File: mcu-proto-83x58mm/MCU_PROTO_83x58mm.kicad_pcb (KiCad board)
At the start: 2 copper layers, 75 x 49 mm, 213 parts, among them J1 Screw_Terminal_01x03, J10 Conn_01x20_Female, J11 Conn_01x01_Male, J12 Conn_01x01_Male, J2 Screw_Terminal_01x03, J3 Conn_01x20_Female, J4 Conn_01x20_Female, J5 Conn_01x20_Female, J6 Conn_01x20_Female, J7 Conn_01x20_Female, J8 Conn_01x20_Female, J9 Conn_01x20_Female

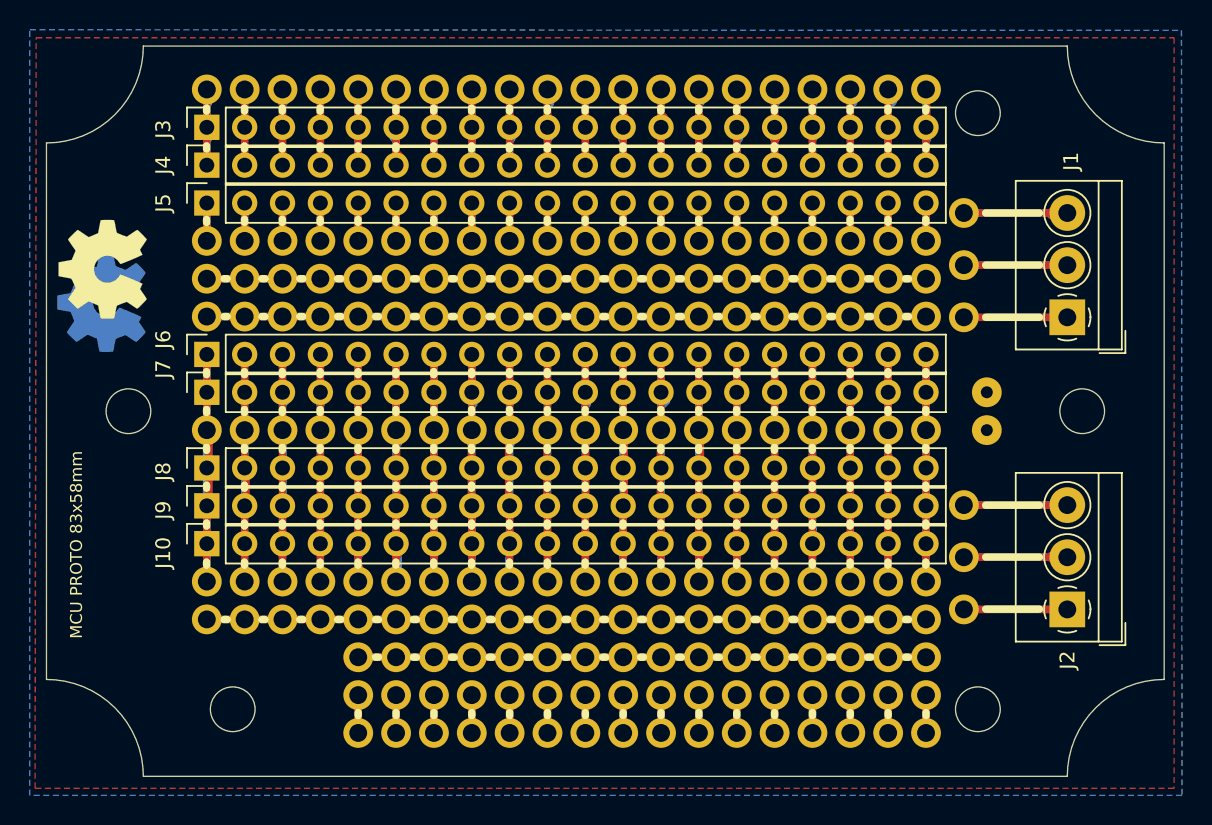
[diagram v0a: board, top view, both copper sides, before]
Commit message: Update MCU_PROTO_83x58mm: PCB improvements and Gerber file regeneration
- Updated main PCB file (MCU_PROTO_83x58mm.kicad_pcb) with design improvements
- Regenerated all Gerber files for single board (copper, mask, silkscreen, drills)
- Updated panel Gerber files with new naming convention
- Replaced old silkscreen files (B_SilkS/F_SilkS) with new Silkscreen versions
- Removed obsolete SVG visualization files
- Added new KiCad project files (.kicad_prl, .kicad_pro, .kicad_sch)
- Added custom library with pad and silkscreen footprints
- Updated footprint library cache and table
- Added backup files from recent design iterations
- Generated new Gerber ZIP archives for single and panel boards
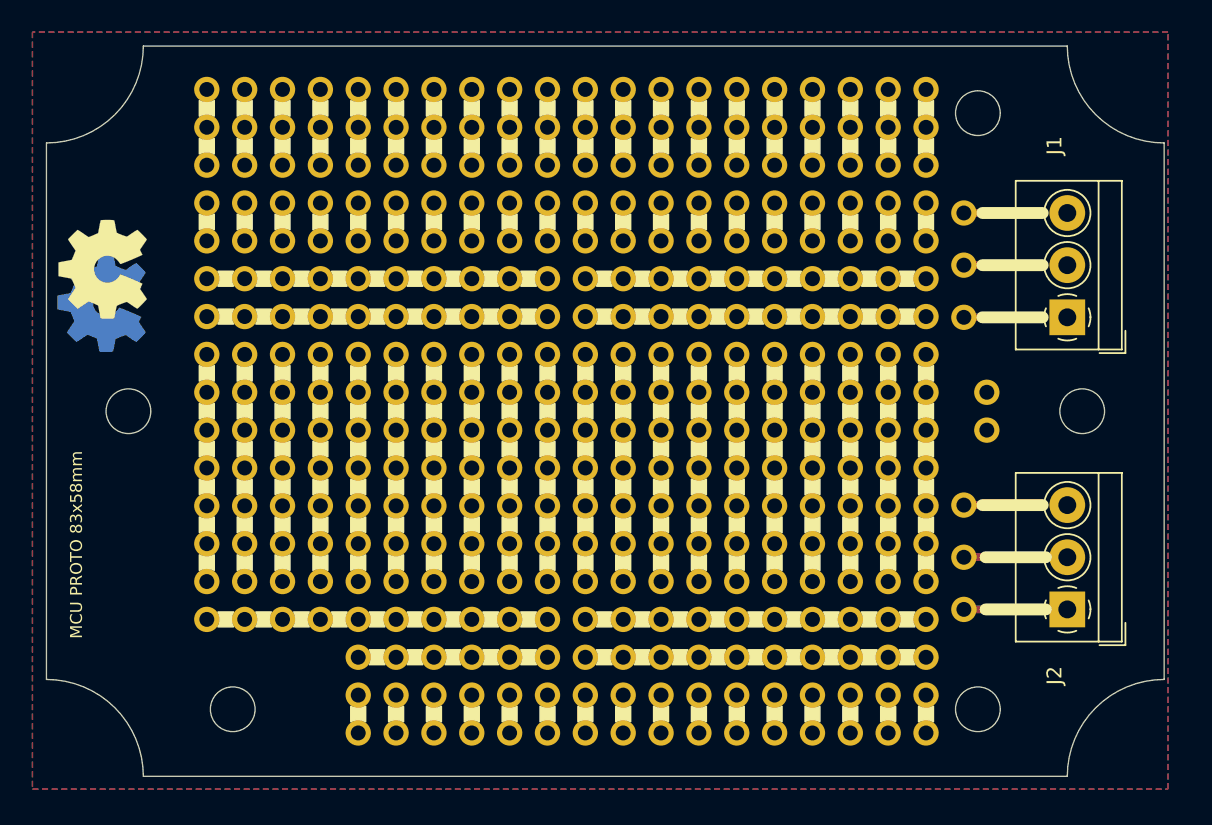
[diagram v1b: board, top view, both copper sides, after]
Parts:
- removed H2, H3, H4, H5, H6: MountingHole, MountingHole:MountingHole_3mm
- removed J10, J3, J4, J5, J6, J7, J8, J9: Conn_01x20_Female, Connector_PinSocket_2.54mm:PinSocket_1x20_P2.54mm_Vertical
- removed the REF** at (110.8, 113.1)
- removed the REF** at (138.7, 125.8)
- removed the REF** at (143.8, 118.2)
- removed the REF** at (141.2, 118.2)
- removed the REF** at (138.7, 118.2)
- removed the REF** at (136.2, 118.2)
- removed the REF** at (133.6, 118.2)
- removed the REF** at (131.1, 118.2)
- removed the REF** at (128.5, 118.2)
- removed the REF** at (126.0, 118.2)
- removed the REF** at (123.5, 118.2)
- removed the REF** at (120.9, 118.2)
- removed the REF** at (136.2, 125.8)
- removed the REF** at (118.4, 118.2)
- removed the REF** at (115.8, 118.2)
- removed the REF** at (113.3, 118.2)
- removed the REF** at (110.8, 118.2)
- removed the REF** at (159.0, 115.6)
- removed the REF** at (156.5, 115.6)
- removed the REF** at (153.9, 115.6)
- removed the REF** at (151.4, 115.6)
- removed the REF** at (148.9, 115.6)
- removed the REF** at (146.3, 115.6)
- removed the REF** at (133.6, 125.8)
- removed the REF** at (143.8, 115.6)
- removed the REF** at (141.2, 115.6)
- removed the REF** at (138.7, 115.6)
- removed the REF** at (136.2, 115.6)
- removed the REF** at (133.6, 115.6)
- removed the REF** at (131.1, 115.6)
- removed the REF** at (128.5, 115.6)
- removed the REF** at (126.0, 115.6)
- removed the REF** at (123.5, 115.6)
- removed the REF** at (120.9, 115.6)
- removed the REF** at (131.1, 125.8)
- removed the REF** at (118.4, 115.6)
- removed the REF** at (115.8, 115.6)
- removed the REF** at (113.3, 115.6)
- removed the REF** at (110.8, 115.6)
- removed the REF** at (159.0, 113.1)
- removed the REF** at (156.5, 113.1)
- removed the REF** at (153.9, 113.1)
- removed the REF** at (151.4, 113.1)
- removed the REF** at (148.9, 113.1)
- removed the REF** at (146.3, 113.1)
- removed the REF** at (128.5, 125.8)
- removed the REF** at (143.8, 113.1)
- removed the REF** at (141.2, 113.1)
- removed the REF** at (138.7, 113.1)
- removed the REF** at (136.2, 113.1)
- removed the REF** at (133.6, 113.1)
- removed the REF** at (131.1, 113.1)
- removed the REF** at (128.5, 113.1)
- removed the REF** at (126.0, 113.1)
- removed the REF** at (123.5, 113.1)
- removed the REF** at (120.9, 113.1)
- removed the REF** at (126.0, 125.8)
- removed the REF** at (118.4, 113.1)
- removed the REF** at (115.8, 113.1)
- removed the REF** at (113.3, 113.1)
- removed the REF** at (110.8, 102.9)
- removed the REF** at (113.3, 102.9)
- removed the REF** at (115.8, 102.9)
- removed the REF** at (118.4, 102.9)
- removed the REF** at (120.9, 102.9)
- removed the REF** at (123.5, 102.9)
- removed the REF** at (123.5, 146.1)
- removed the REF** at (123.5, 125.8)
- removed the REF** at (120.9, 146.1)
- removed the REF** at (159.0, 146.1)
- removed the REF** at (156.5, 146.1)
- removed the REF** at (138.7, 146.1)
- removed the REF** at (146.3, 146.1)
- removed the REF** at (141.2, 146.1)
- removed the REF** at (136.2, 146.1)
- removed the REF** at (133.6, 146.1)
- removed the REF** at (131.1, 146.1)
- removed the REF** at (128.5, 146.1)
- removed the REF** at (120.9, 125.8)
- removed the REF** at (126.0, 146.1)
- removed the REF** at (143.8, 146.1)
- removed the REF** at (148.9, 146.1)
- removed the REF** at (153.9, 146.1)
- removed the REF** at (151.4, 146.1)
- removed the REF** at (146.3, 102.9)
- removed the REF** at (159.0, 102.9)
- removed the REF** at (156.5, 102.9)
- removed the REF** at (153.9, 102.9)
- removed the REF** at (151.4, 102.9)
- removed the REF** at (118.4, 125.8)
- removed the REF** at (148.9, 102.9)
- removed the REF** at (161.6, 114.7)
- removed the REF** at (161.6, 137.8)
- removed the REF** at (161.6, 134.3)
- removed the REF** at (161.6, 130.8)
- removed the REF** at (161.6, 118.2)
- removed the REF** at (161.6, 111.2)
- removed the REF** at (143.8, 102.9)
- removed the REF** at (141.2, 102.9)
- removed the REF** at (138.7, 102.9)
- removed the REF** at (115.8, 125.8)
- removed the REF** at (136.2, 102.9)
- removed the REF** at (133.6, 102.9)
- removed the REF** at (131.1, 102.9)
- removed the REF** at (128.5, 102.9)
- removed the REF** at (126.0, 102.9)
- removed the REF** at (159.0, 125.8)
- removed the REF** at (113.3, 125.8)
- removed the REF** at (110.8, 125.8)
- removed the REF** at (159.0, 143.6)
- removed the REF** at (156.5, 143.6)
- removed the REF** at (153.9, 143.6)
- removed the REF** at (151.4, 143.6)
- removed the REF** at (148.9, 143.6)
- removed the REF** at (146.3, 143.6)
- removed the REF** at (143.8, 143.6)
- removed the REF** at (141.2, 143.6)
- removed the REF** at (156.5, 125.8)
- removed the REF** at (138.7, 143.6)
- removed the REF** at (136.2, 143.6)
- removed the REF** at (133.6, 143.6)
- removed the REF** at (131.1, 143.6)
- removed the REF** at (128.5, 143.6)
- removed the REF** at (126.0, 143.6)
- removed the REF** at (123.5, 143.6)
- removed the REF** at (120.9, 143.6)
- removed the REF** at (159.0, 141.0)
- removed the REF** at (156.5, 141.0)
- removed the REF** at (153.9, 125.8)
- removed the REF** at (153.9, 141.0)
- removed the REF** at (151.4, 141.0)
- removed the REF** at (148.9, 141.0)
- removed the REF** at (146.3, 141.0)
- removed the REF** at (143.8, 141.0)
- removed the REF** at (141.2, 141.0)
- removed the REF** at (138.7, 141.0)
- removed the REF** at (136.2, 141.0)
- removed the REF** at (133.6, 141.0)
- removed the REF** at (131.1, 141.0)
- removed the REF** at (151.4, 125.8)
- removed the REF** at (128.5, 141.0)
- removed the REF** at (126.0, 141.0)
- removed the REF** at (123.5, 141.0)
- removed the REF** at (120.9, 141.0)
- removed the REF** at (159.0, 138.5)
- removed the REF** at (156.5, 138.5)
- removed the REF** at (153.9, 138.5)
- removed the REF** at (151.4, 138.5)
- removed the REF** at (148.9, 138.5)
- removed the REF** at (146.3, 138.5)
- removed the REF** at (148.9, 125.8)
- removed the REF** at (143.8, 138.5)
- removed the REF** at (141.2, 138.5)
- removed the REF** at (138.7, 138.5)
- removed the REF** at (136.2, 138.5)
- removed the REF** at (133.6, 138.5)
- removed the REF** at (131.1, 138.5)
- removed the REF** at (128.5, 138.5)
- removed the REF** at (126.0, 138.5)
- removed the REF** at (123.5, 138.5)
- removed the REF** at (120.9, 138.5)
- removed the REF** at (146.3, 125.8)
- removed the REF** at (118.4, 138.5)
- removed the REF** at (115.8, 138.5)
- removed the REF** at (113.3, 138.5)
- removed the REF** at (110.8, 138.5)
- removed the REF** at (159.0, 135.9)
- removed the REF** at (156.5, 135.9)
- removed the REF** at (153.9, 135.9)
- removed the REF** at (151.4, 135.9)
- removed the REF** at (148.9, 135.9)
- removed the REF** at (146.3, 135.9)
- removed the REF** at (143.8, 125.8)
- removed the REF** at (143.8, 135.9)
- removed the REF** at (141.2, 135.9)
- removed the REF** at (138.7, 135.9)
- removed the REF** at (136.2, 135.9)
- removed the REF** at (133.6, 135.9)
- removed the REF** at (131.1, 135.9)
- removed the REF** at (128.5, 135.9)
- removed the REF** at (126.0, 135.9)
- removed the REF** at (123.5, 135.9)
- removed the REF** at (120.9, 135.9)
- removed the REF** at (141.2, 125.8)
- removed the REF** at (118.4, 135.9)
- removed the REF** at (115.8, 135.9)
- removed the REF** at (113.3, 135.9)
- removed the REF** at (110.8, 135.9)
- removed the REF** at (159.0, 118.2)
- removed the REF** at (156.5, 118.2)
- removed the REF** at (153.9, 118.2)
- removed the REF** at (151.4, 118.2)
- removed the REF** at (148.9, 118.2)
- removed the REF** at (146.3, 118.2)
- added REF**: Round_Pad_1.7mm_Hole_1.0mm, proto-pcb-pads:RoundPad_1.7mm_Hole_1.0mm, F.Cu at (133.6, 118.2)
- added REF**: Pad_Link_1.7mm_Width_1.0mm, proto-pcb-silks:PadLink_1.7mm_Width_1.0mm, F.Cu at (138.7, 130.8)
- added REF**: Round_Pad_1.7mm_Hole_1.0mm, proto-pcb-pads:RoundPad_1.7mm_Hole_1.0mm, F.Cu at (159.0, 141.0)
- added REF**: Round_Pad_1.7mm_Hole_1.0mm, proto-pcb-pads:RoundPad_1.7mm_Hole_1.0mm, F.Cu at (141.2, 146.1)
- added REF**: Round_Pad_1.7mm_Hole_1.0mm, proto-pcb-pads:RoundPad_1.7mm_Hole_1.0mm, F.Cu at (153.9, 125.8)
- added REF**: Round_Pad_1.7mm_Hole_1.0mm, proto-pcb-pads:RoundPad_1.7mm_Hole_1.0mm, F.Cu at (143.8, 143.6)
- added REF**: Round_Pad_1.7mm_Hole_1.0mm, proto-pcb-pads:RoundPad_1.7mm_Hole_1.0mm, F.Cu at (156.5, 115.6)
- added REF**: Round_Pad_1.7mm_Hole_1.0mm, proto-pcb-pads:RoundPad_1.7mm_Hole_1.0mm, F.Cu at (153.9, 141.0)
- added REF**: Pad_Link_1.7mm_Width_1.0mm, proto-pcb-silks:PadLink_1.7mm_Width_1.0mm, F.Cu at (153.9, 138.5)
- added REF**: Round_Pad_1.7mm_Hole_1.0mm, proto-pcb-pads:RoundPad_1.7mm_Hole_1.0mm, F.Cu at (136.2, 123.2)
- added REF**: Round_Pad_1.7mm_Hole_1.0mm, proto-pcb-pads:RoundPad_1.7mm_Hole_1.0mm, F.Cu at (110.8, 135.9)
- added REF**: Round_Pad_1.7mm_Hole_1.0mm, proto-pcb-pads:RoundPad_1.7mm_Hole_1.0mm, F.Cu at (126.0, 123.2)
- added REF**: Pad_Link_1.7mm_Width_1.0mm, proto-pcb-silks:PadLink_1.7mm_Width_1.0mm, F.Cu at (151.4, 115.6)
- added REF**: Pad_Link_1.7mm_Width_1.0mm, proto-pcb-silks:PadLink_1.7mm_Width_1.0mm, F.Cu at (141.2, 141.0)
- added REF**: Pad_Link_1.7mm_Width_1.0mm, proto-pcb-silks:PadLink_1.7mm_Width_1.0mm, F.Cu at (151.4, 141.0)
- added REF**: Pad_Link_1.7mm_Width_1.0mm, proto-pcb-silks:PadLink_1.7mm_Width_1.0mm, F.Cu at (138.7, 105.5)
- added REF**: Pad_Link_1.7mm_Width_1.0mm, proto-pcb-silks:PadLink_1.7mm_Width_1.0mm, F.Cu at (113.3, 120.7)
- added REF**: MountingHole_3mm, MountingHole:MountingHole_3mm, F.Cu at (162.5, 104.5)
- added REF**: Round_Pad_1.7mm_Hole_1.0mm, proto-pcb-pads:RoundPad_1.7mm_Hole_1.0mm, F.Cu at (126.0, 133.4)
- added REF**: Round_Pad_1.7mm_Hole_1.0mm, proto-pcb-pads:RoundPad_1.7mm_Hole_1.0mm, F.Cu at (126.0, 120.7)
- added REF**: Round_Pad_1.7mm_Hole_1.0mm, proto-pcb-pads:RoundPad_1.7mm_Hole_1.0mm, F.Cu at (120.9, 128.3)
- added REF**: Pad_Link_1.7mm_Width_1.0mm, proto-pcb-silks:PadLink_1.7mm_Width_1.0mm, F.Cu at (115.8, 138.5)
- added REF**: Pad_Link_1.7mm_Width_1.0mm, proto-pcb-silks:PadLink_1.7mm_Width_1.0mm, F.Cu at (153.9, 133.4)
- added REF**: Round_Pad_1.7mm_Hole_1.0mm, proto-pcb-pads:RoundPad_1.7mm_Hole_1.0mm, F.Cu at (123.5, 128.3)
- added REF**: Pad_Link_1.7mm_Width_1.0mm, proto-pcb-silks:PadLink_1.7mm_Width_1.0mm, F.Cu at (143.8, 123.2)
- added REF**: Round_Pad_1.7mm_Hole_1.0mm, proto-pcb-pads:RoundPad_1.7mm_Hole_1.0mm, F.Cu at (148.9, 143.6)
- added REF**: Round_Pad_1.7mm_Hole_1.0mm, proto-pcb-pads:RoundPad_1.7mm_Hole_1.0mm, F.Cu at (151.4, 115.6)
- added REF**: Round_Pad_1.7mm_Hole_1.0mm, proto-pcb-pads:RoundPad_1.7mm_Hole_1.0mm, F.Cu at (153.9, 115.6)
- added REF**: Pad_Link_1.7mm_Width_1.0mm, proto-pcb-silks:PadLink_1.7mm_Width_1.0mm, F.Cu at (143.8, 120.7)
- added REF**: Round_Pad_1.7mm_Hole_1.0mm, proto-pcb-pads:RoundPad_1.7mm_Hole_1.0mm, F.Cu at (115.8, 128.3)
- added REF**: Pad_Link_1.7mm_Width_1.0mm, proto-pcb-silks:PadLink_1.7mm_Width_1.0mm, F.Cu at (113.3, 138.5)
- added REF**: Round_Pad_1.7mm_Hole_1.0mm, proto-pcb-pads:RoundPad_1.7mm_Hole_1.0mm, F.Cu at (136.2, 125.8)
- added REF**: Pad_Link_1.7mm_Width_1.0mm, proto-pcb-silks:PadLink_1.7mm_Width_1.0mm, F.Cu at (128.5, 125.8)
- added REF**: Pad_Link_1.7mm_Width_1.0mm, proto-pcb-silks:PadLink_1.7mm_Width_1.0mm, F.Cu at (151.4, 123.2)
- added REF**: Pad_Link_1.7mm_Width_1.0mm, proto-pcb-silks:PadLink_1.7mm_Width_1.0mm, F.Cu at (123.5, 133.4)
- added REF**: Pad_Link_1.7mm_Width_1.0mm, proto-pcb-silks:PadLink_1.7mm_Width_1.0mm, F.Cu at (131.1, 123.2)
- added REF**: Pad_Link_1.7mm_Width_1.0mm, proto-pcb-silks:PadLink_1.7mm_Width_1.0mm, F.Cu at (110.8, 128.3)
- added REF**: Round_Pad_1.7mm_Hole_1.0mm, proto-pcb-pads:RoundPad_1.7mm_Hole_1.0mm, F.Cu at (120.9, 102.9)
- added REF**: Pad_Link_1.7mm_Width_1.0mm, proto-pcb-silks:PadLink_1.7mm_Width_1.0mm, F.Cu at (133.6, 102.9)
- added REF**: Round_Pad_1.7mm_Hole_1.0mm, proto-pcb-pads:RoundPad_1.7mm_Hole_1.0mm, F.Cu at (146.3, 102.9)
- added REF**: Pad_Link_1.7mm_Width_1.0mm, proto-pcb-silks:PadLink_1.7mm_Width_1.0mm, F.Cu at (148.9, 138.5)
- added REF**: Round_Pad_1.7mm_Hole_1.0mm, proto-pcb-pads:RoundPad_1.7mm_Hole_1.0mm, F.Cu at (148.9, 146.1)
- added REF**: Pad_Link_1.7mm_Width_1.0mm, proto-pcb-silks:PadLink_1.7mm_Width_1.0mm, F.Cu at (133.6, 105.5)
- added REF**: Pad_Link_1.7mm_Width_1.0mm, proto-pcb-silks:PadLink_1.7mm_Width_1.0mm, F.Cu at (113.3, 110.5)
- added REF**: Pad_Link_1.7mm_Width_1.0mm, proto-pcb-silks:PadLink_1.7mm_Width_1.0mm, F.Cu at (118.4, 123.2)
- added REF**: Round_Pad_1.7mm_Hole_1.0mm, proto-pcb-pads:RoundPad_1.7mm_Hole_1.0mm, F.Cu at (141.2, 128.3)
- added REF**: Round_Pad_1.7mm_Hole_1.0mm, proto-pcb-pads:RoundPad_1.7mm_Hole_1.0mm, F.Cu at (110.8, 128.3)
- added REF**: Pad_Link_1.7mm_Width_1.0mm, proto-pcb-silks:PadLink_1.7mm_Width_1.0mm, F.Cu at (159.0, 102.9)
- added REF**: Pad_Link_1.7mm_Width_1.0mm, proto-pcb-silks:PadLink_1.7mm_Width_1.0mm, F.Cu at (159.0, 105.5)
- added REF**: Round_Pad_1.7mm_Hole_1.0mm, proto-pcb-pads:RoundPad_1.7mm_Hole_1.0mm, F.Cu at (136.2, 146.1)
- added REF**: Round_Pad_1.7mm_Hole_1.0mm, proto-pcb-pads:RoundPad_1.7mm_Hole_1.0mm, F.Cu at (148.9, 138.5)
- added REF**: Pad_Link_1.7mm_Width_1.0mm, proto-pcb-silks:PadLink_1.7mm_Width_1.0mm, F.Cu at (123.5, 110.5)
- added REF**: Pad_Link_1.7mm_Width_1.0mm, proto-pcb-silks:PadLink_1.7mm_Width_1.0mm, F.Cu at (143.8, 133.4)
- added REF**: Round_Pad_1.7mm_Hole_1.0mm, proto-pcb-pads:RoundPad_1.7mm_Hole_1.0mm, F.Cu at (131.1, 108.0)
- added REF**: Round_Pad_1.7mm_Hole_1.0mm, proto-pcb-pads:RoundPad_1.7mm_Hole_1.0mm, F.Cu at (146.3, 108.0)
- added REF**: Round_Pad_1.7mm_Hole_1.0mm, proto-pcb-pads:RoundPad_1.7mm_Hole_1.0mm, F.Cu at (146.3, 138.5)
- added REF**: Pad_Link_1.7mm_Width_1.0mm, proto-pcb-silks:PadLink_1.7mm_Width_1.0mm, F.Cu at (120.9, 125.8)
- added REF**: Round_Pad_1.7mm_Hole_1.0mm, proto-pcb-pads:RoundPad_1.7mm_Hole_1.0mm, F.Cu at (128.5, 105.5)
- added REF**: Round_Pad_1.7mm_Hole_1.0mm, proto-pcb-pads:RoundPad_1.7mm_Hole_1.0mm, F.Cu at (156.5, 108.0)
- added REF**: Round_Pad_1.7mm_Hole_1.0mm, proto-pcb-pads:RoundPad_1.7mm_Hole_1.0mm, F.Cu at (128.5, 146.1)
- added REF**: Pad_Link_1.7mm_Width_1.0mm, proto-pcb-silks:PadLink_1.7mm_Width_1.0mm, F.Cu at (128.5, 123.2)
- added REF**: Pad_Link_1.7mm_Width_1.0mm, proto-pcb-silks:PadLink_1.7mm_Width_1.0mm, F.Cu at (123.5, 123.2)
- added REF**: Pad_Link_1.7mm_Width_1.0mm, proto-pcb-silks:PadLink_1.7mm_Width_1.0mm, F.Cu at (131.1, 130.8)
- added REF**: Round_Pad_1.7mm_Hole_1.0mm, proto-pcb-pads:RoundPad_1.7mm_Hole_1.0mm, F.Cu at (141.2, 125.8)
- added REF**: Round_Pad_1.7mm_Hole_1.0mm, proto-pcb-pads:RoundPad_1.7mm_Hole_1.0mm, F.Cu at (120.9, 143.6)
- added REF**: Round_Pad_1.7mm_Hole_1.0mm, proto-pcb-pads:RoundPad_1.7mm_Hole_1.0mm, F.Cu at (141.2, 120.7)
- added REF**: Pad_Link_1.7mm_Width_1.0mm, proto-pcb-silks:PadLink_1.7mm_Width_1.0mm, F.Cu at (146.3, 128.3)
- added REF**: Pad_Link_1.7mm_Width_1.0mm, proto-pcb-silks:PadLink_1.7mm_Width_1.0mm, F.Cu at (123.5, 102.9)
- added REF**: Pad_Link_1.7mm_Width_1.0mm, proto-pcb-silks:PadLink_1.7mm_Width_1.0mm, F.Cu at (148.9, 143.6)
- added REF**: Round_Pad_1.7mm_Hole_1.0mm, proto-pcb-pads:RoundPad_1.7mm_Hole_1.0mm, F.Cu at (123.5, 120.7)
- added REF**: Pad_Link_1.7mm_Width_1.0mm, proto-pcb-silks:PadLink_1.7mm_Width_1.0mm, F.Cu at (148.9, 120.7)
- added REF**: Round_Pad_1.7mm_Hole_1.0mm, proto-pcb-pads:RoundPad_1.7mm_Hole_1.0mm, F.Cu at (146.3, 105.5)
- added REF**: Round_Pad_1.7mm_Hole_1.0mm, proto-pcb-pads:RoundPad_1.7mm_Hole_1.0mm, F.Cu at (126.0, 113.1)
- added REF**: Pad_Link_1.7mm_Width_1.0mm, proto-pcb-silks:PadLink_1.7mm_Width_1.0mm, F.Cu at (151.4, 133.4)
- added REF**: Pad_Link_1.7mm_Width_1.0mm, proto-pcb-silks:PadLink_1.7mm_Width_1.0mm, F.Cu at (153.9, 125.8)
- added REF**: Round_Pad_1.7mm_Hole_1.0mm, proto-pcb-pads:RoundPad_1.7mm_Hole_1.0mm, F.Cu at (153.9, 143.6)
- added REF**: Round_Pad_1.7mm_Hole_1.0mm, proto-pcb-pads:RoundPad_1.7mm_Hole_1.0mm, F.Cu at (133.6, 123.2)
- added REF**: Pad_Link_1.7mm_Width_1.0mm, proto-pcb-silks:PadLink_1.7mm_Width_1.0mm, F.Cu at (148.9, 102.9)
- added REF**: Pad_Link_1.7mm_Width_1.0mm, proto-pcb-silks:PadLink_1.7mm_Width_1.0mm, F.Cu at (146.3, 125.8)
- added REF**: Round_Pad_1.7mm_Hole_1.0mm, proto-pcb-pads:RoundPad_1.7mm_Hole_1.0mm, F.Cu at (128.5, 115.6)
- added REF**: Pad_Link_1.7mm_Width_1.0mm, proto-pcb-silks:PadLink_1.7mm_Width_1.0mm, F.Cu at (128.5, 133.4)
- added REF**: Pad_Link_1.7mm_Width_1.0mm, proto-pcb-silks:PadLink_1.7mm_Width_1.0mm, F.Cu at (143.8, 125.8)
- added REF**: Pad_Link_1.7mm_Width_1.0mm, proto-pcb-silks:PadLink_1.7mm_Width_1.0mm, F.Cu at (156.5, 143.6)
- added REF**: Round_Pad_1.7mm_Hole_1.0mm, proto-pcb-pads:RoundPad_1.7mm_Hole_1.0mm, F.Cu at (153.9, 135.9)
- added REF**: Round_Pad_1.7mm_Hole_1.0mm, proto-pcb-pads:RoundPad_1.7mm_Hole_1.0mm, F.Cu at (120.9, 105.5)
- added REF**: Pad_Link_1.7mm_Width_1.0mm, proto-pcb-silks:PadLink_1.7mm_Width_1.0mm, F.Cu at (141.2, 110.5)
- added REF**: Round_Pad_1.7mm_Hole_1.0mm, proto-pcb-pads:RoundPad_1.7mm_Hole_1.0mm, F.Cu at (133.6, 113.1)
- added REF**: Round_Pad_1.7mm_Hole_1.0mm, proto-pcb-pads:RoundPad_1.7mm_Hole_1.0mm, F.Cu at (128.5, 141.0)
- added REF**: Pad_Link_1.7mm_Width_1.0mm, proto-pcb-silks:PadLink_1.7mm_Width_1.0mm, F.Cu at (120.9, 128.3)
- added REF**: Pad_Link_1.7mm_Width_1.0mm, proto-pcb-silks:PadLink_1.7mm_Width_1.0mm, F.Cu at (146.3, 102.9)
- added REF**: Round_Pad_1.7mm_Hole_1.0mm, proto-pcb-pads:RoundPad_1.7mm_Hole_1.0mm, F.Cu at (159.0, 105.5)
- added REF**: Pad_Link_1.7mm_Width_1.0mm, proto-pcb-silks:PadLink_1.7mm_Width_1.0mm, F.Cu at (113.3, 105.5)
- added REF**: Pad_Link_1.7mm_Width_1.0mm, proto-pcb-silks:PadLink_1.7mm_Width_1.0mm, F.Cu at (153.9, 123.2)
- added REF**: Round_Pad_1.7mm_Hole_1.0mm, proto-pcb-pads:RoundPad_1.7mm_Hole_1.0mm, F.Cu at (141.2, 115.6)
- added REF**: Round_Pad_1.7mm_Hole_1.0mm, proto-pcb-pads:RoundPad_1.7mm_Hole_1.0mm, F.Cu at (120.9, 115.6)
- added REF**: Round_Pad_1.7mm_Hole_1.0mm, proto-pcb-pads:RoundPad_1.7mm_Hole_1.0mm, F.Cu at (123.5, 130.8)
- added REF**: Round_Pad_1.7mm_Hole_1.0mm, proto-pcb-pads:RoundPad_1.7mm_Hole_1.0mm, F.Cu at (153.9, 110.5)
- added REF**: Pad_Link_1.7mm_Width_1.0mm, proto-pcb-silks:PadLink_1.7mm_Width_1.0mm, F.Cu at (113.3, 125.8)
- added REF**: Round_Pad_1.7mm_Hole_1.0mm, proto-pcb-pads:RoundPad_1.7mm_Hole_1.0mm, F.Cu at (151.4, 105.5)
- added REF**: Round_Pad_1.7mm_Hole_1.0mm, proto-pcb-pads:RoundPad_1.7mm_Hole_1.0mm, F.Cu at (113.3, 105.5)
- added REF**: Round_Pad_1.7mm_Hole_1.0mm, proto-pcb-pads:RoundPad_1.7mm_Hole_1.0mm, F.Cu at (159.0, 138.5)
- added REF**: Pad_Link_1.7mm_Width_1.0mm, proto-pcb-silks:PadLink_1.7mm_Width_1.0mm, F.Cu at (156.5, 115.6)
- added REF**: Pad_Link_1.7mm_Width_1.0mm, proto-pcb-silks:PadLink_1.7mm_Width_1.0mm, F.Cu at (156.5, 118.2)
- added REF**: Pad_Link_1.7mm_Width_1.0mm, proto-pcb-silks:PadLink_1.7mm_Width_1.0mm, F.Cu at (126.0, 128.3)
- added REF**: Round_Pad_1.7mm_Hole_1.0mm, proto-pcb-pads:RoundPad_1.7mm_Hole_1.0mm, F.Cu at (115.8, 123.2)
- added REF**: Round_Pad_1.7mm_Hole_1.0mm, proto-pcb-pads:RoundPad_1.7mm_Hole_1.0mm, F.Cu at (113.3, 128.3)
- added REF**: Round_Pad_1.7mm_Hole_1.0mm, proto-pcb-pads:RoundPad_1.7mm_Hole_1.0mm, F.Cu at (143.8, 113.1)
- added REF**: Round_Pad_1.7mm_Hole_1.0mm, proto-pcb-pads:RoundPad_1.7mm_Hole_1.0mm, F.Cu at (146.3, 135.9)
- added REF**: Round_Pad_1.7mm_Hole_1.0mm, proto-pcb-pads:RoundPad_1.7mm_Hole_1.0mm, F.Cu at (156.5, 105.5)
- added REF**: Pad_Link_1.7mm_Width_1.0mm, proto-pcb-silks:PadLink_1.7mm_Width_1.0mm, F.Cu at (151.4, 138.5)
- added REF**: Round_Pad_1.7mm_Hole_1.0mm, proto-pcb-pads:RoundPad_1.7mm_Hole_1.0mm, F.Cu at (143.8, 130.8)
- added REF**: Round_Pad_1.7mm_Hole_1.0mm, proto-pcb-pads:RoundPad_1.7mm_Hole_1.0mm, F.Cu at (113.3, 125.8)
- added REF**: Pad_Link_1.7mm_Width_1.0mm, proto-pcb-silks:PadLink_1.7mm_Width_1.0mm, F.Cu at (126.0, 110.5)
- added REF**: Round_Pad_1.7mm_Hole_1.0mm, proto-pcb-pads:RoundPad_1.7mm_Hole_1.0mm, F.Cu at (128.5, 120.7)
- added REF**: Pad_Link_1.7mm_Width_1.0mm, proto-pcb-silks:PadLink_1.7mm_Width_1.0mm, F.Cu at (110.8, 133.4)
- added REF**: Pad_Link_1.7mm_Width_1.0mm, proto-pcb-silks:PadLink_1.7mm_Width_1.0mm, F.Cu at (118.4, 128.3)
- added REF**: Pad_Link_1.7mm_Width_1.0mm, proto-pcb-silks:PadLink_1.7mm_Width_1.0mm, F.Cu at (123.5, 105.5)
- added REF**: Pad_Link_1.7mm_Width_1.0mm, proto-pcb-silks:PadLink_1.7mm_Width_1.0mm, F.Cu at (136.2, 130.8)
- added REF**: Pad_Link_1.7mm_Width_1.0mm, proto-pcb-silks:PadLink_1.7mm_Width_1.0mm, F.Cu at (138.7, 120.7)
- added REF**: Round_Pad_1.7mm_Hole_1.0mm, proto-pcb-pads:RoundPad_1.7mm_Hole_1.0mm, F.Cu at (143.8, 133.4)
- added REF**: Round_Pad_1.7mm_Hole_1.0mm, proto-pcb-pads:RoundPad_1.7mm_Hole_1.0mm, F.Cu at (146.3, 128.3)
- added REF**: Round_Pad_1.7mm_Hole_1.0mm, proto-pcb-pads:RoundPad_1.7mm_Hole_1.0mm, F.Cu at (133.6, 128.3)
- added REF**: Round_Pad_1.7mm_Hole_1.0mm, proto-pcb-pads:RoundPad_1.7mm_Hole_1.0mm, F.Cu at (146.3, 110.5)
- added REF**: Round_Pad_1.7mm_Hole_1.0mm, proto-pcb-pads:RoundPad_1.7mm_Hole_1.0mm, F.Cu at (131.1, 118.2)
- added REF**: Round_Pad_1.7mm_Hole_1.0mm, proto-pcb-pads:RoundPad_1.7mm_Hole_1.0mm, F.Cu at (148.9, 120.7)
- added REF**: Pad_Link_1.7mm_Width_1.0mm, proto-pcb-silks:PadLink_1.7mm_Width_1.0mm, F.Cu at (123.5, 125.8)
- added REF**: Pad_Link_1.7mm_Width_1.0mm, proto-pcb-silks:PadLink_1.7mm_Width_1.0mm, F.Cu at (133.6, 125.8)
- added REF**: Round_Pad_1.7mm_Hole_1.0mm, proto-pcb-pads:RoundPad_1.7mm_Hole_1.0mm, F.Cu at (120.9, 133.4)
- added REF**: Round_Pad_1.7mm_Hole_1.0mm, proto-pcb-pads:RoundPad_1.7mm_Hole_1.0mm, F.Cu at (146.3, 130.8)
- added REF**: Pad_Link_1.7mm_Width_1.0mm, proto-pcb-silks:PadLink_1.7mm_Width_1.0mm, F.Cu at (118.4, 115.6)
- added REF**: Round_Pad_1.7mm_Hole_1.0mm, proto-pcb-pads:RoundPad_1.7mm_Hole_1.0mm, F.Cu at (146.3, 120.7)
- added REF**: Pad_Link_1.7mm_Width_1.0mm, proto-pcb-silks:PadLink_1.7mm_Width_1.0mm, F.Cu at (138.7, 133.4)
- added REF**: Round_Pad_1.7mm_Hole_1.0mm, proto-pcb-pads:RoundPad_1.7mm_Hole_1.0mm, F.Cu at (138.7, 143.6)
- added REF**: Round_Pad_1.7mm_Hole_1.0mm, proto-pcb-pads:RoundPad_1.7mm_Hole_1.0mm, F.Cu at (115.8, 108.0)
- added REF**: Round_Pad_1.7mm_Hole_1.0mm, proto-pcb-pads:RoundPad_1.7mm_Hole_1.0mm, F.Cu at (136.2, 118.2)
- added REF**: Round_Pad_1.7mm_Hole_1.0mm, proto-pcb-pads:RoundPad_1.7mm_Hole_1.0mm, F.Cu at (136.2, 115.6)
- added REF**: Round_Pad_1.7mm_Hole_1.0mm, proto-pcb-pads:RoundPad_1.7mm_Hole_1.0mm, F.Cu at (123.5, 143.6)
- added REF**: Round_Pad_1.7mm_Hole_1.0mm, proto-pcb-pads:RoundPad_1.7mm_Hole_1.0mm, F.Cu at (133.6, 143.6)
- added REF**: Round_Pad_1.7mm_Hole_1.0mm, proto-pcb-pads:RoundPad_1.7mm_Hole_1.0mm, F.Cu at (131.1, 113.1)
- added REF**: Pad_Link_1.7mm_Width_1.0mm, proto-pcb-silks:PadLink_1.7mm_Width_1.0mm, F.Cu at (138.7, 115.6)
- added REF**: Pad_Link_1.7mm_Width_1.0mm, proto-pcb-silks:PadLink_1.7mm_Width_1.0mm, F.Cu at (159.0, 133.4)
- added REF**: Pad_Link_1.7mm_Width_1.0mm, proto-pcb-silks:PadLink_1.7mm_Width_1.0mm, F.Cu at (136.2, 133.4)
- added REF**: Pad_Link_1.7mm_Width_1.0mm, proto-pcb-silks:PadLink_1.7mm_Width_1.0mm, F.Cu at (133.6, 130.8)
- added REF**: Round_Pad_1.7mm_Hole_1.0mm, proto-pcb-pads:RoundPad_1.7mm_Hole_1.0mm, F.Cu at (153.9, 133.4)
- added REF**: Round_Pad_1.7mm_Hole_1.0mm, proto-pcb-pads:RoundPad_1.7mm_Hole_1.0mm, F.Cu at (133.6, 102.9)
- added REF**: Pad_Link_1.7mm_Width_1.0mm, proto-pcb-silks:PadLink_1.7mm_Width_1.0mm, F.Cu at (153.9, 102.9)
- added REF**: Round_Pad_1.7mm_Hole_1.0mm, proto-pcb-pads:RoundPad_1.7mm_Hole_1.0mm, F.Cu at (148.9, 113.1)
- added REF**: Pad_Link_1.7mm_Width_1.0mm, proto-pcb-silks:PadLink_1.7mm_Width_1.0mm, F.Cu at (126.0, 118.2)
- added REF**: Round_Pad_1.7mm_Hole_1.0mm, proto-pcb-pads:RoundPad_1.7mm_Hole_1.0mm, F.Cu at (159.0, 115.6)
- added REF**: Pad_Link_1.7mm_Width_1.0mm, proto-pcb-silks:PadLink_1.7mm_Width_1.0mm, F.Cu at (110.8, 115.6)
- added REF**: Round_Pad_1.7mm_Hole_1.0mm, proto-pcb-pads:RoundPad_1.7mm_Hole_1.0mm, F.Cu at (159.0, 113.1)
- added REF**: Pad_Link_1.7mm_Width_1.0mm, proto-pcb-silks:PadLink_1.7mm_Width_1.0mm, F.Cu at (133.6, 120.7)
- added REF**: Round_Pad_1.7mm_Hole_1.0mm, proto-pcb-pads:RoundPad_1.7mm_Hole_1.0mm, F.Cu at (136.2, 130.8)
- added REF**: Pad_Link_1.7mm_Width_1.0mm, proto-pcb-silks:PadLink_1.7mm_Width_1.0mm, F.Cu at (138.7, 138.5)
- added REF**: Pad_Link_1.7mm_Width_1.0mm, proto-pcb-silks:PadLink_1.7mm_Width_1.0mm, F.Cu at (131.1, 128.3)
- added REF**: Round_Pad_1.7mm_Hole_1.0mm, proto-pcb-pads:RoundPad_1.7mm_Hole_1.0mm, F.Cu at (156.5, 146.1)
- added REF**: Round_Pad_1.7mm_Hole_1.0mm, proto-pcb-pads:RoundPad_1.7mm_Hole_1.0mm, F.Cu at (131.1, 125.8)
- added REF**: Round_Pad_1.7mm_Hole_1.0mm, proto-pcb-pads:RoundPad_1.7mm_Hole_1.0mm, F.Cu at (143.8, 128.3)
- added REF**: Round_Pad_1.7mm_Hole_1.0mm, proto-pcb-pads:RoundPad_1.7mm_Hole_1.0mm, F.Cu at (128.5, 128.3)
- added REF**: Round_Pad_1.7mm_Hole_1.0mm, proto-pcb-pads:RoundPad_1.7mm_Hole_1.0mm, F.Cu at (156.5, 120.7)
- added REF**: Round_Pad_1.7mm_Hole_1.0mm, proto-pcb-pads:RoundPad_1.7mm_Hole_1.0mm, F.Cu at (113.3, 110.5)
- added REF**: Pad_Link_1.7mm_Width_1.0mm, proto-pcb-silks:PadLink_1.7mm_Width_1.0mm, F.Cu at (128.5, 130.8)
- added REF**: Round_Pad_1.7mm_Hole_1.0mm, proto-pcb-pads:RoundPad_1.7mm_Hole_1.0mm, F.Cu at (159.0, 135.9)
- added REF**: Round_Pad_1.7mm_Hole_1.0mm, proto-pcb-pads:RoundPad_1.7mm_Hole_1.0mm, F.Cu at (143.8, 141.0)
- added REF**: Round_Pad_1.7mm_Hole_1.0mm, proto-pcb-pads:RoundPad_1.7mm_Hole_1.0mm, F.Cu at (126.0, 135.9)
- added REF**: Pad_Link_1.7mm_Width_1.0mm, proto-pcb-silks:PadLink_1.7mm_Width_1.0mm, F.Cu at (136.2, 123.2)
- added REF**: Pad_Link_1.7mm_Width_1.0mm, proto-pcb-silks:PadLink_1.7mm_Width_1.0mm, F.Cu at (113.3, 115.6)
- added REF**: Round_Pad_1.7mm_Hole_1.0mm, proto-pcb-pads:RoundPad_1.7mm_Hole_1.0mm, F.Cu at (115.8, 135.9)
- added REF**: Round_Pad_1.7mm_Hole_1.0mm, proto-pcb-pads:RoundPad_1.7mm_Hole_1.0mm, F.Cu at (148.9, 133.4)
- added REF**: Round_Pad_1.7mm_Hole_1.0mm, proto-pcb-pads:RoundPad_1.7mm_Hole_1.0mm, F.Cu at (110.8, 138.5)
- added REF**: Round_Pad_1.7mm_Hole_1.0mm, proto-pcb-pads:RoundPad_1.7mm_Hole_1.0mm, F.Cu at (151.4, 120.7)
- added REF**: Pad_Link_1.7mm_Width_1.0mm, proto-pcb-silks:PadLink_1.7mm_Width_1.0mm, F.Cu at (151.4, 120.7)
- added REF**: Pad_Link_1.7mm_Width_1.0mm, proto-pcb-silks:PadLink_1.7mm_Width_1.0mm, F.Cu at (133.6, 123.2)
- added REF**: Pad_Link_1.7mm_Width_1.0mm, proto-pcb-silks:PadLink_1.7mm_Width_1.0mm, F.Cu at (138.7, 118.2)
- added REF**: Round_Pad_1.7mm_Hole_1.0mm, proto-pcb-pads:RoundPad_1.7mm_Hole_1.0mm, F.Cu at (118.4, 138.5)
- added REF**: Round_Pad_1.7mm_Hole_1.0mm, proto-pcb-pads:RoundPad_1.7mm_Hole_1.0mm, F.Cu at (151.4, 130.8)
- added REF**: Pad_Link_1.7mm_Width_1.0mm, proto-pcb-silks:PadLink_1.7mm_Width_1.0mm, F.Cu at (126.0, 123.2)
- added REF**: Round_Pad_1.7mm_Hole_1.0mm, proto-pcb-pads:RoundPad_1.7mm_Hole_1.0mm, F.Cu at (151.4, 128.3)
- added REF**: MountingHole_3mm, MountingHole:MountingHole_3mm, F.Cu at (169.5, 124.5)
- added REF**: Pad_Link_1.7mm_Width_1.0mm, proto-pcb-silks:PadLink_1.7mm_Width_1.0mm, F.Cu at (133.6, 143.6)
- added REF**: Round_Pad_1.7mm_Hole_1.0mm, proto-pcb-pads:RoundPad_1.7mm_Hole_1.0mm, F.Cu at (151.4, 123.2)
- added REF**: Round_Pad_1.7mm_Hole_1.0mm, proto-pcb-pads:RoundPad_1.7mm_Hole_1.0mm, F.Cu at (153.9, 108.0)
- added REF**: Round_Pad_1.7mm_Hole_1.0mm, proto-pcb-pads:RoundPad_1.7mm_Hole_1.0mm, F.Cu at (115.8, 105.5)
- added REF**: Round_Pad_1.7mm_Hole_1.0mm, proto-pcb-pads:RoundPad_1.7mm_Hole_1.0mm, F.Cu at (141.2, 130.8)
- added REF**: Round_Pad_1.7mm_Hole_1.0mm, proto-pcb-pads:RoundPad_1.7mm_Hole_1.0mm, F.Cu at (148.9, 135.9)
- added REF**: Round_Pad_1.7mm_Hole_1.0mm, proto-pcb-pads:RoundPad_1.7mm_Hole_1.0mm, F.Cu at (118.4, 128.3)
- added REF**: Pad_Link_1.7mm_Width_1.0mm, proto-pcb-silks:PadLink_1.7mm_Width_1.0mm, F.Cu at (156.5, 105.5)
- added REF**: Round_Pad_1.7mm_Hole_1.0mm, proto-pcb-pads:RoundPad_1.7mm_Hole_1.0mm, F.Cu at (133.6, 120.7)
- added REF**: Round_Pad_1.7mm_Hole_1.0mm, proto-pcb-pads:RoundPad_1.7mm_Hole_1.0mm, F.Cu at (138.7, 113.1)
- added REF**: Round_Pad_1.7mm_Hole_1.0mm, proto-pcb-pads:RoundPad_1.7mm_Hole_1.0mm, F.Cu at (138.7, 105.5)
- added REF**: Round_Pad_1.7mm_Hole_1.0mm, proto-pcb-pads:RoundPad_1.7mm_Hole_1.0mm, F.Cu at (123.5, 138.5)
- added REF**: Round_Pad_1.7mm_Hole_1.0mm, proto-pcb-pads:RoundPad_1.7mm_Hole_1.0mm, F.Cu at (128.5, 130.8)
- added REF**: Pad_Link_1.7mm_Width_1.0mm, proto-pcb-silks:PadLink_1.7mm_Width_1.0mm, F.Cu at (146.3, 138.5)
- added REF**: Round_Pad_1.7mm_Hole_1.0mm, proto-pcb-pads:RoundPad_1.7mm_Hole_1.0mm, F.Cu at (141.2, 110.5)
- added REF**: Pad_Link_1.7mm_Width_1.0mm, proto-pcb-silks:PadLink_1.7mm_Width_1.0mm, F.Cu at (120.9, 138.5)
- added REF**: Pad_Link_1.7mm_Width_1.0mm, proto-pcb-silks:PadLink_1.7mm_Width_1.0mm, F.Cu at (151.4, 130.8)
- added REF**: Round_Pad_1.7mm_Hole_1.0mm, proto-pcb-pads:RoundPad_1.7mm_Hole_1.0mm, F.Cu at (151.4, 108.0)
- added REF**: Pad_Link_1.7mm_Width_1.0mm, proto-pcb-silks:PadLink_1.7mm_Width_1.0mm, F.Cu at (146.3, 120.7)
- added REF**: Round_Pad_1.7mm_Hole_1.0mm, proto-pcb-pads:RoundPad_1.7mm_Hole_1.0mm, F.Cu at (115.8, 138.5)
- added REF**: Pad_Link_1.7mm_Width_1.0mm, proto-pcb-silks:PadLink_1.7mm_Width_1.0mm, F.Cu at (159.0, 123.2)
- added REF**: Pad_Link_1.7mm_Width_1.0mm, proto-pcb-silks:PadLink_1.7mm_Width_1.0mm, F.Cu at (143.8, 118.2)
- added REF**: Round_Pad_1.7mm_Hole_1.0mm, proto-pcb-pads:RoundPad_1.7mm_Hole_1.0mm, F.Cu at (143.8, 138.5)
- added REF**: Pad_Link_1.7mm_Width_1.0mm, proto-pcb-silks:PadLink_1.7mm_Width_1.0mm, F.Cu at (126.0, 143.6)
- added REF**: Pad_Link_1.7mm_Width_1.0mm, proto-pcb-silks:PadLink_1.7mm_Width_1.0mm, F.Cu at (131.1, 105.5)
- added REF**: Pad_Link_1.7mm_Width_1.0mm, proto-pcb-silks:PadLink_1.7mm_Width_1.0mm, F.Cu at (131.1, 138.5)
- added REF**: Round_Pad_1.7mm_Hole_1.0mm, proto-pcb-pads:RoundPad_1.7mm_Hole_1.0mm, F.Cu at (118.4, 105.5)
- added REF**: Round_Pad_1.7mm_Hole_1.0mm, proto-pcb-pads:RoundPad_1.7mm_Hole_1.0mm, F.Cu at (133.6, 133.4)
- added REF**: Pad_Link_1.7mm_Width_1.0mm, proto-pcb-silks:PadLink_1.7mm_Width_1.0mm, F.Cu at (115.8, 123.2)
- added REF**: Round_Pad_1.7mm_Hole_1.0mm, proto-pcb-pads:RoundPad_1.7mm_Hole_1.0mm, F.Cu at (161.6, 118.2)
- added REF**: Pad_Link_1.7mm_Width_1.0mm, proto-pcb-silks:PadLink_1.7mm_Width_1.0mm, F.Cu at (153.9, 105.5)
- added REF**: Pad_Link_1.7mm_Width_1.0mm, proto-pcb-silks:PadLink_1.7mm_Width_1.0mm, F.Cu at (113.3, 123.2)
- added REF**: Pad_Link_1.7mm_Width_1.0mm, proto-pcb-silks:PadLink_1.7mm_Width_1.0mm, F.Cu at (123.5, 138.5)
- added REF**: Pad_Link_1.7mm_Width_1.0mm, proto-pcb-silks:PadLink_1.7mm_Width_1.0mm, F.Cu at (133.6, 128.3)
- added REF**: Pad_Link_1.7mm_Width_1.0mm, proto-pcb-silks:PadLink_1.7mm_Width_1.0mm, F.Cu at (118.4, 130.8)
- added REF**: Round_Pad_1.7mm_Hole_1.0mm, proto-pcb-pads:RoundPad_1.7mm_Hole_1.0mm, F.Cu at (110.8, 113.1)
- added REF**: Round_Pad_1.7mm_Hole_1.0mm, proto-pcb-pads:RoundPad_1.7mm_Hole_1.0mm, F.Cu at (115.8, 130.8)
- added REF**: Round_Pad_1.7mm_Hole_1.0mm, proto-pcb-pads:RoundPad_1.7mm_Hole_1.0mm, F.Cu at (128.5, 135.9)
- added REF**: Pad_Link_1.7mm_Width_1.0mm, proto-pcb-silks:PadLink_1.7mm_Width_1.0mm, F.Cu at (138.7, 125.8)
- added REF**: Pad_Link_1.7mm_Width_1.0mm, proto-pcb-silks:PadLink_1.7mm_Width_1.0mm, F.Cu at (146.3, 143.6)
- added REF**: Pad_Link_1.7mm_Width_1.0mm, proto-pcb-silks:PadLink_1.7mm_Width_1.0mm, F.Cu at (146.3, 130.8)
- added REF**: Pad_Link_1.7mm_Width_1.0mm, proto-pcb-silks:PadLink_1.7mm_Width_1.0mm, F.Cu at (156.5, 123.2)
- added REF**: Pad_Link_1.7mm_Width_1.0mm, proto-pcb-silks:PadLink_1.7mm_Width_1.0mm, F.Cu at (153.9, 128.3)
- added REF**: Round_Pad_1.7mm_Hole_1.0mm, proto-pcb-pads:RoundPad_1.7mm_Hole_1.0mm, F.Cu at (138.7, 125.8)
- added REF**: Round_Pad_1.7mm_Hole_1.0mm, proto-pcb-pads:RoundPad_1.7mm_Hole_1.0mm, F.Cu at (143.8, 123.2)
- added REF**: Pad_Link_1.7mm_Width_1.0mm, proto-pcb-silks:PadLink_1.7mm_Width_1.0mm, F.Cu at (113.3, 128.3)
- added REF**: Round_Pad_1.7mm_Hole_1.0mm, proto-pcb-pads:RoundPad_1.7mm_Hole_1.0mm, F.Cu at (161.6, 114.7)
- added REF**: Pad_Link_1.7mm_Width_1.0mm, proto-pcb-silks:PadLink_1.7mm_Width_1.0mm, F.Cu at (113.3, 102.9)
- added REF**: Pad_Link_1.7mm_Width_1.0mm, proto-pcb-silks:PadLink_1.7mm_Width_1.0mm, F.Cu at (151.4, 110.5)
- added REF**: MountingHole_3mm, MountingHole:MountingHole_3mm, F.Cu at (162.5, 144.5)
- added REF**: Pad_Link_1.7mm_Width_1.0mm, proto-pcb-silks:PadLink_1.7mm_Width_1.0mm, F.Cu at (159.0, 110.5)
- added REF**: Pad_Link_1.7mm_Width_1.0mm, proto-pcb-silks:PadLink_1.7mm_Width_1.0mm, F.Cu at (151.4, 143.6)
- added REF**: Pad_Link_1.7mm_Width_1.0mm, proto-pcb-silks:PadLink_1.7mm_Width_1.0mm, F.Cu at (136.2, 120.7)
- added REF**: Pad_Link_1.7mm_Width_1.0mm, proto-pcb-silks:PadLink_1.7mm_Width_1.0mm, F.Cu at (153.9, 115.6)
- added REF**: Round_Pad_1.7mm_Hole_1.0mm, proto-pcb-pads:RoundPad_1.7mm_Hole_1.0mm, F.Cu at (126.0, 138.5)
- added REF**: Pad_Link_1.7mm_Width_1.0mm, proto-pcb-silks:PadLink_1.7mm_Width_1.0mm, F.Cu at (128.5, 115.6)
- added REF**: Pad_Link_1.7mm_Width_1.0mm, proto-pcb-silks:PadLink_1.7mm_Width_1.0mm, F.Cu at (131.1, 102.9)
- added REF**: Pad_Link_1.7mm_Width_1.0mm, proto-pcb-silks:PadLink_1.7mm_Width_1.0mm, F.Cu at (110.8, 123.2)
- added REF**: Pad_Link_1.7mm_Width_1.0mm, proto-pcb-silks:PadLink_1.7mm_Width_1.0mm, F.Cu at (123.5, 141.0)
- added REF**: Round_Pad_1.7mm_Hole_1.0mm, proto-pcb-pads:RoundPad_1.7mm_Hole_1.0mm, F.Cu at (141.2, 113.1)
- added REF**: Pad_Link_1.7mm_Width_1.0mm, proto-pcb-silks:PadLink_1.7mm_Width_1.0mm, F.Cu at (153.9, 118.2)
- added REF**: Pad_Link_1.7mm_Width_1.0mm, proto-pcb-silks:PadLink_1.7mm_Width_1.0mm, F.Cu at (113.3, 118.2)
- added REF**: Round_Pad_1.7mm_Hole_1.0mm, proto-pcb-pads:RoundPad_1.7mm_Hole_1.0mm, F.Cu at (131.1, 105.5)
- added REF**: Round_Pad_1.7mm_Hole_1.0mm, proto-pcb-pads:RoundPad_1.7mm_Hole_1.0mm, F.Cu at (110.8, 115.6)
- added REF**: Round_Pad_1.7mm_Hole_1.0mm, proto-pcb-pads:RoundPad_1.7mm_Hole_1.0mm, F.Cu at (151.4, 141.0)
- added REF**: Pad_Link_1.7mm_Width_1.0mm, proto-pcb-silks:PadLink_1.7mm_Width_1.0mm, F.Cu at (115.8, 120.7)
- added REF**: Round_Pad_1.7mm_Hole_1.0mm, proto-pcb-pads:RoundPad_1.7mm_Hole_1.0mm, F.Cu at (161.6, 111.2)
- added REF**: Round_Pad_1.7mm_Hole_1.0mm, proto-pcb-pads:RoundPad_1.7mm_Hole_1.0mm, F.Cu at (123.5, 102.9)
- added REF**: Round_Pad_1.7mm_Hole_1.0mm, proto-pcb-pads:RoundPad_1.7mm_Hole_1.0mm, F.Cu at (133.6, 130.8)
- added REF**: Round_Pad_1.7mm_Hole_1.0mm, proto-pcb-pads:RoundPad_1.7mm_Hole_1.0mm, F.Cu at (120.9, 141.0)
- added REF**: Round_Pad_1.7mm_Hole_1.0mm, proto-pcb-pads:RoundPad_1.7mm_Hole_1.0mm, F.Cu at (115.8, 113.1)
- added REF**: Pad_Link_1.7mm_Width_1.0mm, proto-pcb-silks:PadLink_1.7mm_Width_1.0mm, F.Cu at (118.4, 138.5)
- added REF**: Pad_Link_1.7mm_Width_1.0mm, proto-pcb-silks:PadLink_1.7mm_Width_1.0mm, F.Cu at (148.9, 110.5)
- added REF**: Round_Pad_1.7mm_Hole_1.0mm, proto-pcb-pads:RoundPad_1.7mm_Hole_1.0mm, F.Cu at (123.5, 105.5)
- added REF**: Round_Pad_1.7mm_Hole_1.0mm, proto-pcb-pads:RoundPad_1.7mm_Hole_1.0mm, F.Cu at (118.4, 115.6)
- added REF**: Round_Pad_1.7mm_Hole_1.0mm, proto-pcb-pads:RoundPad_1.7mm_Hole_1.0mm, F.Cu at (131.1, 138.5)
- added REF**: Round_Pad_1.7mm_Hole_1.0mm, proto-pcb-pads:RoundPad_1.7mm_Hole_1.0mm, F.Cu at (143.8, 146.1)
- added REF**: Pad_Link_1.7mm_Width_1.0mm, proto-pcb-silks:PadLink_1.7mm_Width_1.0mm, F.Cu at (128.5, 105.5)
- added REF**: Round_Pad_1.7mm_Hole_1.0mm, proto-pcb-pads:RoundPad_1.7mm_Hole_1.0mm, F.Cu at (120.9, 118.2)
- added REF**: Round_Pad_1.7mm_Hole_1.0mm, proto-pcb-pads:RoundPad_1.7mm_Hole_1.0mm, F.Cu at (126.0, 110.5)
- added REF**: Round_Pad_1.7mm_Hole_1.0mm, proto-pcb-pads:RoundPad_1.7mm_Hole_1.0mm, F.Cu at (151.4, 102.9)
- added REF**: Round_Pad_1.7mm_Hole_1.0mm, proto-pcb-pads:RoundPad_1.7mm_Hole_1.0mm, F.Cu at (133.6, 125.8)
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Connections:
- net Net-(J11-Pad1) renamed GND
- J1 pad 1: Net-(J1-Pad1) -> unconnected-(J1-Pin_1-Pad1)
- J1 pad 2: Net-(J1-Pad2) -> unconnected-(J1-Pin_2-Pad2)
- J1 pad 3: Net-(J1-Pad3) -> unconnected-(J1-Pin_3-Pad3)
- J2 pad 1: Net-(J2-Pad1) -> unconnected-(J2-Pin_1-Pad1)
- J2 pad 2: Net-(J2-Pad2) -> unconnected-(J2-Pin_2-Pad2)
- J2 pad 3: Net-(J2-Pad3) -> unconnected-(J2-Pin_3-Pad3)
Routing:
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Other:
- net class Default removed
- net class slimstack removed
- rule pad_to_mask_clearance: 0.051 -> 0
